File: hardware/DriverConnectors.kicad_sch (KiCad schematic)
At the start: 12 parts

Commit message: Convert SCH files to latest version. Fix DRC Warnings in PrntrBoard.
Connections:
- net ~ST1_ALARM renamed ~{ST1_ALARM}
- net ~ST1_CS renamed ~{ST1_CS}
- net ~ST2_ALARM renamed ~{ST2_ALARM}
- net ~ST2_CS renamed ~{ST2_CS}
- net ~ST3_ALARM renamed ~{ST3_ALARM}
- net ~ST3_CS renamed ~{ST3_CS}
- net ~ST4_ALARM renamed ~{ST4_ALARM}
- net ~ST4_CS renamed ~{ST4_CS}
- net ~ST5_ALARM renamed ~{ST5_ALARM}
- net ~ST5_CS renamed ~{ST5_CS}
- net ~ST6_ALARM renamed ~{ST6_ALARM}
- net ~ST6_CS renamed ~{ST6_CS}
- net ~ST_ENABLE renamed ~{ST_ENABLE}
- net ~ST_RESET renamed ~{ST_RESET}
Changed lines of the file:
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@@
-(kicad_sch (version 20210126) (generator eeschema)
+(kicad_sch (version 20210621) (generator eeschema)
   (paper "A4")
   (junction (at 42.545 61.595) (diameter 1.016) (color 0 0 0 0))
@@
     )
   )
-  (global_label "~ST_ENABLE" (shape input) (at 38.735 33.655 180)
-    (effects (font (size 1.27 1.27)) (justify right))
-    (property "Intersheet References" "${INTERSHEET_REFS}" (id 0) (at 0 0 0)
-      (effects (font (size 1.27 1.27)) hide)
-    )
-  )
-  (global_label "~ST1_ALARM" (shape input) (at 38.735 36.83 180)
-    (effects (font (size 1.27 1.27)) (justify right))
-    (property "Intersheet References" "${INTERSHEET_REFS}" (id 0) (at 0 0 0)
-      (effects (font (size 1.27 1.27)) hide)
-    )
-  )
-  (global_label "~ST_RESET" (shape input) (at 38.735 40.005 180)
+  (global_label "~{ST_ENABLE}" (shape input) (at 38.735 33.655 180)
+    (effects (font (size 1.27 1.27)) (justify right))
+    (property "Intersheet References" "${INTERSHEET_REFS}" (id 0) (at 0 0 0)
+      (effects (font (size 1.27 1.27)) hide)
+    )
+  )
+  (global_label "~{ST1_ALARM}" (shape input) (at 38.735 36.83 180)
+    (effects (font (size 1.27 1.27)) (justify right))
+    (property "Intersheet References" "${INTERSHEET_REFS}" (id 0) (at 0 0 0)
+      (effects (font (size 1.27 1.27)) hide)
+    )
+  )
+  (global_label "~{ST_RESET}" (shape input) (at 38.735 40.005 180)
     (effects (font (size 1.27 1.27)) (justify right))
     (property "Intersheet References" "${INTERSHEET_REFS}" (id 0) (at 0 0 0)
@@
     )
   )
-  (global_label "~ST_ENABLE" (shape input) (at 39.37 97.79 180)
-    (effects (font (size 1.27 1.27)) (justify right))
-    (property "Intersheet References" "${INTERSHEET_REFS}" (id 0) (at 0 0 0)
-      (effects (font (size 1.27 1.27)) hide)
-    )
-  )
-  (global_label "~ST5_ALARM" (shape input) (at 39.37 100.965 180)
-    (effects (font (size 1.27 1.27)) (justify right))
-    (property "Intersheet References" "${INTERSHEET_REFS}" (id 0) (at 0 0 0)
-      (effects (font (size 1.27 1.27)) hide)
-    )
-  )
-  (global_label "~ST_RESET" (shape input) (at 39.37 104.14 180)
+  (global_label "~{ST_ENABLE}" (shape input) (at 39.37 97.79 180)
+    (effects (font (size 1.27 1.27)) (justify right))
+    (property "Intersheet References" "${INTERSHEET_REFS}" (id 0) (at 0 0 0)
+      (effects (font (size 1.27 1.27)) hide)
+    )
+  )
+  (global_label "~{ST5_ALARM}" (shape input) (at 39.37 100.965 180)
+    (effects (font (size 1.27 1.27)) (justify right))
+    (property "Intersheet References" "${INTERSHEET_REFS}" (id 0) (at 0 0 0)
+      (effects (font (size 1.27 1.27)) hide)
+    )
+  )
+  (global_label "~{ST_RESET}" (shape input) (at 39.37 104.14 180)
     (effects (font (size 1.27 1.27)) (justify right))
     (property "Intersheet References" "${INTERSHEET_REFS}" (id 0) (at 0 0 0)
@@
     )
   )
-  (global_label "~ST1_CS" (shape input) (at 71.755 27.94 0)
+  (global_label "~{ST1_CS}" (shape input) (at 71.755 27.94 0)
     (effects (font (size 1.27 1.27)) (justify left))
     (property "Intersheet References" "${INTERSHEET_REFS}" (id 0) (at 0 0 0)
@@
     )
   )
-  (global_label "~ST5_CS" (shape input) (at 72.39 92.075 0)
+  (global_label "~{ST5_CS}" (shape input) (at 72.39 92.075 0)
     (effects (font (size 1.27 1.27)) (justify left))
     (property "Intersheet References" "${INTERSHEET_REFS}" (id 0) (at 0 0 0)
@@
     )
   )
-  (global_label "~ST_ENABLE" (shape input) (at 100.965 33.02 180)
-    (effects (font (size 1.27 1.27)) (justify right))
-    (property "Intersheet References" "${INTERSHEET_REFS}" (id 0) (at 0 0 0)
-      (effects (font (size 1.27 1.27)) hide)
-    )
-  )
-  (global_label "~ST2_ALARM" (shape input) (at 100.965 36.195 180)
-    (effects (font (size 1.27 1.27)) (justify right))
-    (property "Intersheet References" "${INTERSHEET_REFS}" (id 0) (at 0 0 0)
-      (effects (font (size 1.27 1.27)) hide)
-    )
-  )
-  (global_label "~ST_RESET" (shape input) (at 100.965 39.37 180)
+  (global_label "~{ST_ENABLE}" (shape input) (at 100.965 33.02 180)
+    (effects (font (size 1.27 1.27)) (justify right))
+    (property "Intersheet References" "${INTERSHEET_REFS}" (id 0) (at 0 0 0)
+      (effects (font (size 1.27 1.27)) hide)
+    )
+  )
+  (global_label "~{ST2_ALARM}" (shape input) (at 100.965 36.195 180)
+    (effects (font (size 1.27 1.27)) (justify right))
+    (property "Intersheet References" "${INTERSHEET_REFS}" (id 0) (at 0 0 0)
+      (effects (font (size 1.27 1.27)) hide)
+    )
+  )
+  (global_label "~{ST_RESET}" (shape input) (at 100.965 39.37 180)
     (effects (font (size 1.27 1.27)) (justify right))
     (property "Intersheet References" "${INTERSHEET_REFS}" (id 0) (at 0 0 0)
@@
     )
   )
-  (global_label "~ST_ENABLE" (shape input) (at 101.6 97.155 180)
-    (effects (font (size 1.27 1.27)) (justify right))
-    (property "Intersheet References" "${INTERSHEET_REFS}" (id 0) (at 0 0 0)
-      (effects (font (size 1.27 1.27)) hide)
-    )
-  )
-  (global_label "~ST6_ALARM" (shape input) (at 101.6 100.33 180)
-    (effects (font (size 1.27 1.27)) (justify right))
-    (property "Intersheet References" "${INTERSHEET_REFS}" (id 0) (at 0 0 0)
-      (effects (font (size 1.27 1.27)) hide)
-    )
-  )
-  (global_label "~ST_RESET" (shape input) (at 101.6 103.505 180)
+  (global_label "~{ST_ENABLE}" (shape input) (at 101.6 97.155 180)
+    (effects (font (size 1.27 1.27)) (justify right))
+    (property "Intersheet References" "${INTERSHEET_REFS}" (id 0) (at 0 0 0)
+      (effects (font (size 1.27 1.27)) hide)
+    )
+  )
+  (global_label "~{ST6_ALARM}" (shape input) (at 101.6 100.33 180)
+    (effects (font (size 1.27 1.27)) (justify right))
+    (property "Intersheet References" "${INTERSHEET_REFS}" (id 0) (at 0 0 0)
+      (effects (font (size 1.27 1.27)) hide)
+    )
+  )
+  (global_label "~{ST_RESET}" (shape input) (at 101.6 103.505 180)
     (effects (font (size 1.27 1.27)) (justify right))
     (property "Intersheet References" "${INTERSHEET_REFS}" (id 0) (at 0 0 0)
@@
     )
   )
-  (global_label "~ST2_CS" (shape input) (at 133.985 27.305 0)
+  (global_label "~{ST2_CS}" (shape input) (at 133.985 27.305 0)
     (effects (font (size 1.27 1.27)) (justify left))
     (property "Intersheet References" "${INTERSHEET_REFS}" (id 0) (at 0 0 0)
@@
     )
   )
-  (global_label "~ST6_CS" (shape input) (at 134.62 91.44 0)
+  (global_label "~{ST6_CS}" (shape input) (at 134.62 91.44 0)
     (effects (font (size 1.27 1.27)) (justify left))
     (property "Intersheet References" "${INTERSHEET_REFS}" (id 0) (at 0 0 0)
@@
     )
   )
-  (global_label "~ST_ENABLE" (shape input) (at 161.925 33.02 180)
-    (effects (font (size 1.27 1.27)) (justify right))
-    (property "Intersheet References" "${INTERSHEET_REFS}" (id 0) (at 0 0 0)
-      (effects (font (size 1.27 1.27)) hide)
-    )
-  )
-  (global_label "~ST3_ALARM" (shape input) (at 161.925 36.195 180)
-    (effects (font (size 1.27 1.27)) (justify right))
-    (property "Intersheet References" "${INTERSHEET_REFS}" (id 0) (at 0 0 0)
-      (effects (font (size 1.27 1.27)) hide)
-    )
-  )
-  (global_label "~ST_RESET" (shape input) (at 161.925 39.37 180)
+  (global_label "~{ST_ENABLE}" (shape input) (at 161.925 33.02 180)
+    (effects (font (size 1.27 1.27)) (justify right))
+    (property "Intersheet References" "${INTERSHEET_REFS}" (id 0) (at 0 0 0)
+      (effects (font (size 1.27 1.27)) hide)
+    )
+  )
+  (global_label "~{ST3_ALARM}" (shape input) (at 161.925 36.195 180)
+    (effects (font (size 1.27 1.27)) (justify right))
+    (property "Intersheet References" "${INTERSHEET_REFS}" (id 0) (at 0 0 0)
+      (effects (font (size 1.27 1.27)) hide)
+    )
+  )
+  (global_label "~{ST_RESET}" (shape input) (at 161.925 39.37 180)
     (effects (font (size 1.27 1.27)) (justify right))
     (property "Intersheet References" "${INTERSHEET_REFS}" (id 0) (at 0 0 0)
@@
     )
   )
-  (global_label "~ST3_CS" (shape input) (at 194.945 27.305 0)
+  (global_label "~{ST3_CS}" (shape input) (at 194.945 27.305 0)
     (effects (font (size 1.27 1.27)) (justify left))
     (property "Intersheet References" "${INTERSHEET_REFS}" (id 0) (at 0 0 0)
@@
     )
   )
-  (global_label "~ST_ENABLE" (shape input) (at 227.965 33.02 180)
-    (effects (font (size 1.27 1.27)) (justify right))
-    (property "Intersheet References" "${INTERSHEET_REFS}" (id 0) (at 0 0 0)
-      (effects (font (size 1.27 1.27)) hide)
-    )
-  )
-  (global_label "~ST4_ALARM" (shape input) (at 227.965 36.195 180)
-    (effects (font (size 1.27 1.27)) (justify right))
-    (property "Intersheet References" "${INTERSHEET_REFS}" (id 0) (at 0 0 0)
-      (effects (font (size 1.27 1.27)) hide)
-    )
-  )
-  (global_label "~ST_RESET" (shape input) (at 227.965 39.37 180)
+  (global_label "~{ST_ENABLE}" (shape input) (at 227.965 33.02 180)
+    (effects (font (size 1.27 1.27)) (justify right))
+    (property "Intersheet References" "${INTERSHEET_REFS}" (id 0) (at 0 0 0)
+      (effects (font (size 1.27 1.27)) hide)
+    )
+  )
+  (global_label "~{ST4_ALARM}" (shape input) (at 227.965 36.195 180)
+    (effects (font (size 1.27 1.27)) (justify right))
+    (property "Intersheet References" "${INTERSHEET_REFS}" (id 0) (at 0 0 0)
+      (effects (font (size 1.27 1.27)) hide)
+    )
+  )
+  (global_label "~{ST_RESET}" (shape input) (at 227.965 39.37 180)
     (effects (font (size 1.27 1.27)) (justify right))
     (property "Intersheet References" "${INTERSHEET_REFS}" (id 0) (at 0 0 0)
@@
     )
   )
-  (global_label "~ST4_CS" (shape input) (at 260.985 27.305 0)
-    (effects (font (size 1.27 1.27)) (justify left))
-    (property "Intersheet References" "${INTERSHEET_REFS}" (id 0) (at 0 0 0)
+  (global_label "~{ST4_CS}" (shape input) (at 260.985 27.305 0)
+    (effects (font (size 1.27 1.27)) (justify left))
+    (property "Intersheet References" "${INTERSHEET_REFS}" (id 0) (at 0 0 0)

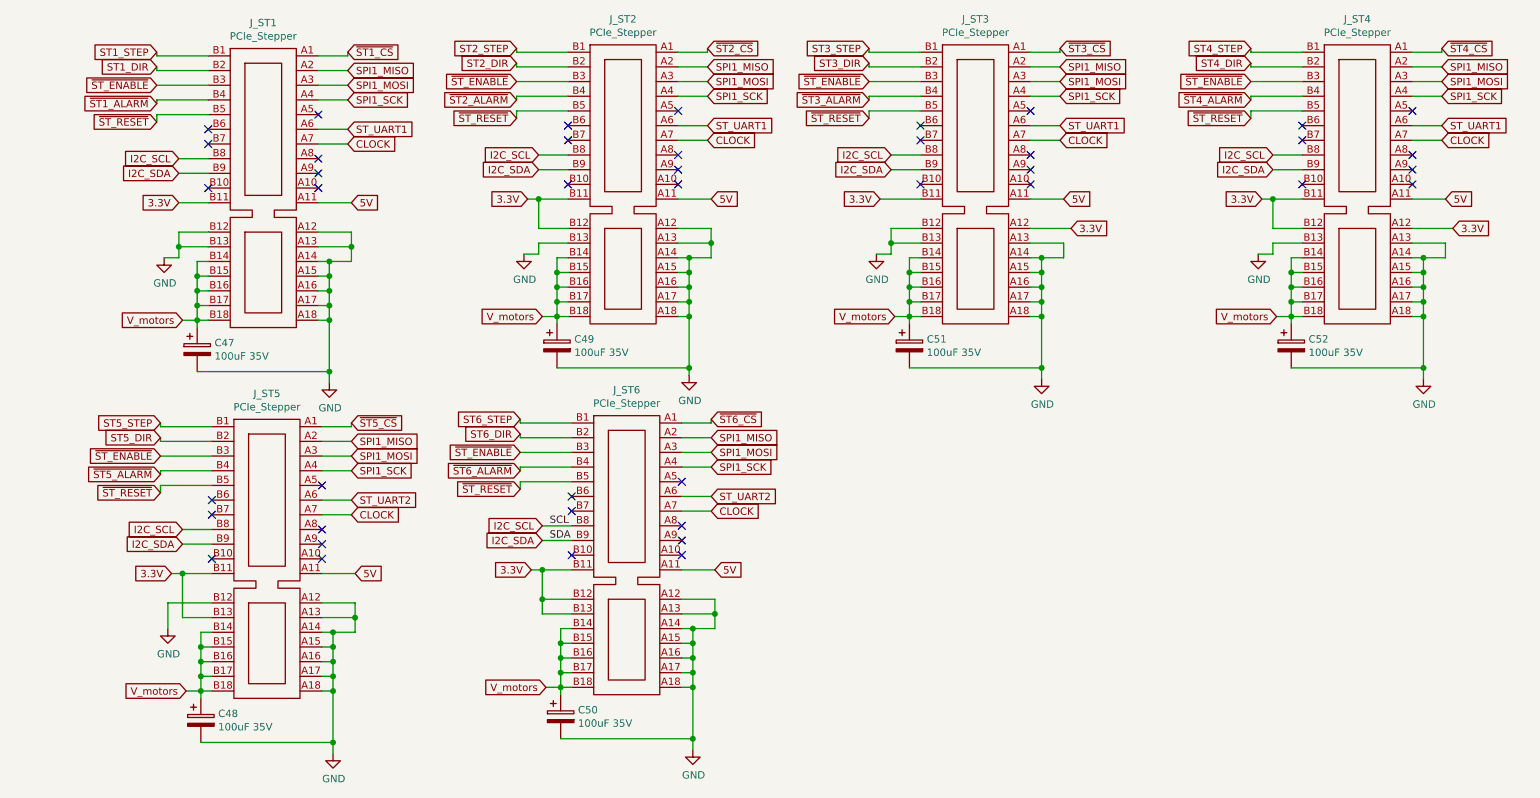
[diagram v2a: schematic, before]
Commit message: Added separate power supply for motor drivers, to accomodate high voltage driver versions.
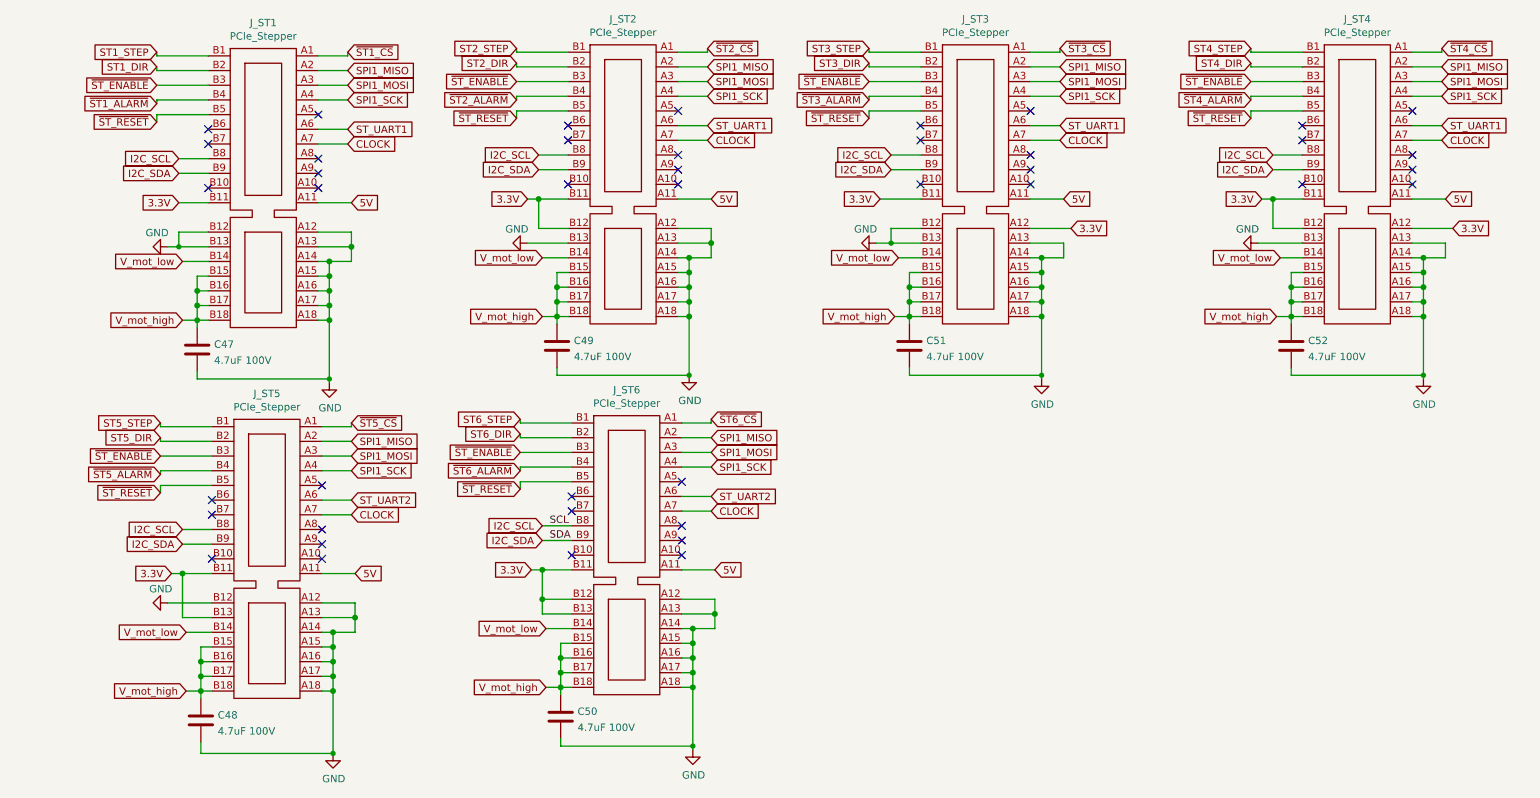
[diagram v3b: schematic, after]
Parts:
- removed C47, C48, C49, C50, C51, C52: 100uF 35V, Capacitor_SMD:CP_Elec_6.3x7.7, symbol Device:CP
- added C47, C48, C49, C50, C51, C52: 4.7uF 100V, Capacitor_SMD:C_1210_3225Metric, symbol Device:C
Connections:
- net GND: now also C47.2, C48.2, C49.2, C50.2, C51.2, C52.2
- net V_motors renamed V_mot_high
- net V_mot_high: now also C47.1, C48.1, C49.1, C50.1, C51.1, C52.1; no longer J_ST1.B14, J_ST2.B14, J_ST3.B14, J_ST4.B14, J_ST5.B14, J_ST6.B14
- new net V_mot_low: J_ST1.B14, J_ST2.B14, J_ST3.B14, J_ST4.B14, J_ST5.B14, J_ST6.B14

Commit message: Add voltage selection for each stepper driver.
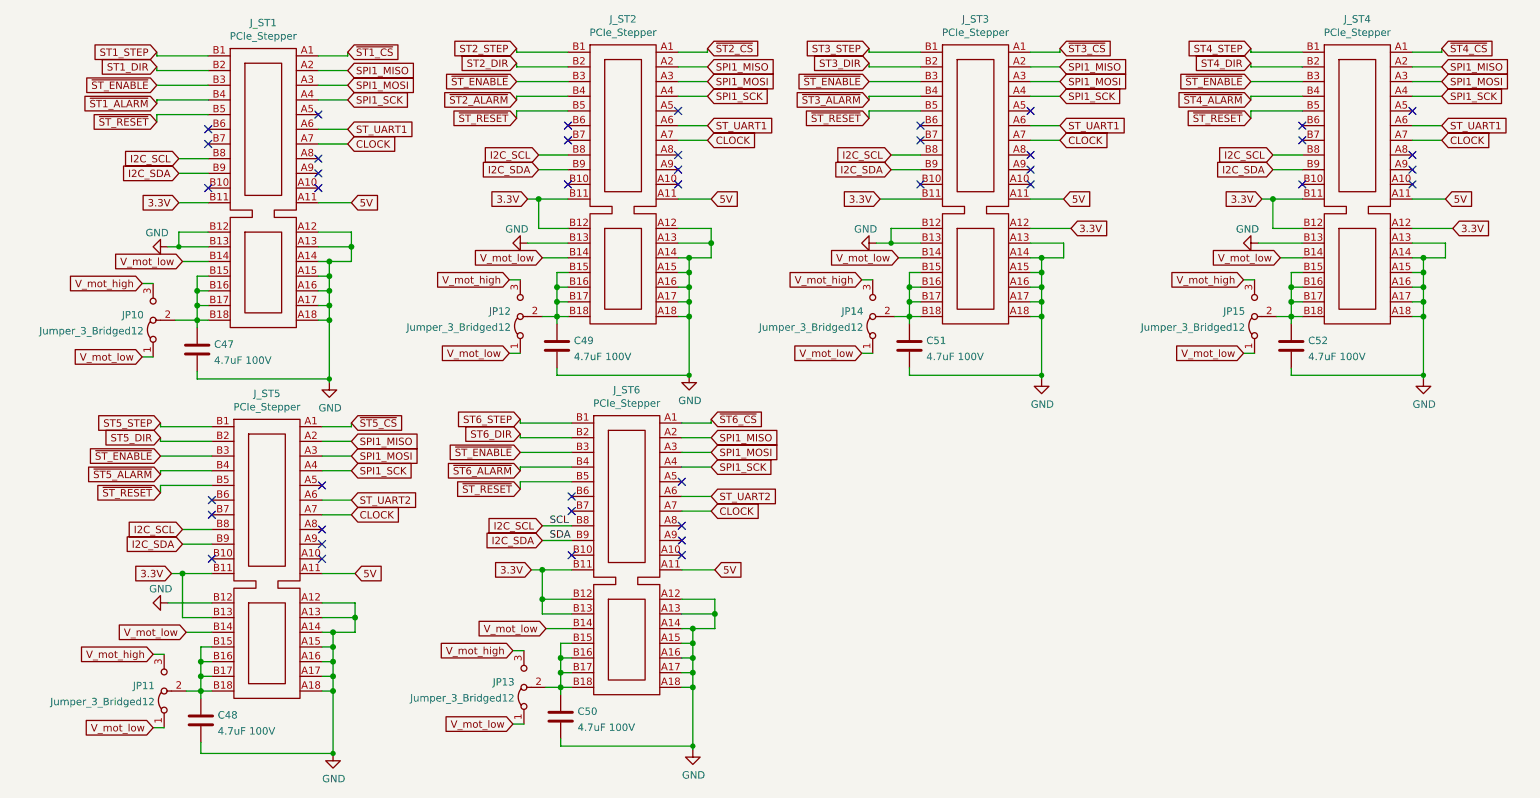
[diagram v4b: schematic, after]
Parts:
- added JP10, JP11, JP12, JP13, JP14, JP15: Jumper_3_Bridged12, Connector_PinHeader_2.54mm:PinHeader_1x03_P2.54mm_Vertical, symbol Jumper:Jumper_3_Bridged12
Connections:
- net V_mot_high: now also JP10.3 (B), JP11.3 (B), JP12.3 (B), JP13.3 (B), JP14.3 (B), JP15.3 (B); no longer C47.1, C48.1, C49.1, C50.1, C51.1, C52.1, J_ST1.B15, J_ST1.B16, J_ST1.B17, J_ST1.B18, J_ST2.B15, J_ST2.B16, J_ST2.B17, J_ST2.B18, J_ST3.B15, J_ST3.B16, J_ST3.B17, J_ST3.B18, J_ST4.B15, J_ST4.B16, J_ST4.B17, J_ST4.B18, J_ST5.B15, J_ST5.B16, J_ST5.B17, J_ST5.B18, J_ST6.B15, J_ST6.B16, J_ST6.B17, J_ST6.B18
- net V_mot_low: now also JP10.1 (A), JP11.1 (A), JP12.1 (A), JP13.1 (A), JP14.1 (A), JP15.1 (A)
- new net: C49.1, JP12.2 (C), J_ST2.B15, J_ST2.B16, J_ST2.B17, J_ST2.B18
- new net: C51.1, JP14.2 (C), J_ST3.B15, J_ST3.B16, J_ST3.B17, J_ST3.B18
- new net: C52.1, JP15.2 (C), J_ST4.B15, J_ST4.B16, J_ST4.B17, J_ST4.B18
- new net: C48.1, JP11.2 (C), J_ST5.B15, J_ST5.B16, J_ST5.B17, J_ST5.B18
- new net: C50.1, JP13.2 (C), J_ST6.B15, J_ST6.B16, J_ST6.B17, J_ST6.B18
- new net: C47.1, JP10.2 (C), J_ST1.B15, J_ST1.B16, J_ST1.B17, J_ST1.B18
